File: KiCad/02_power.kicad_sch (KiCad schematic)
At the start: 48 parts, among them IC201 MCP73831T-2ACI_OT, J201 Barrel_Jack_Switch_Pin3Ring, J202 BM02B-GHS-TBT_LF__SN__N_, Q201 DMG3415U-7, U201 AMS1117-3.3, U202 TLV62569DBV

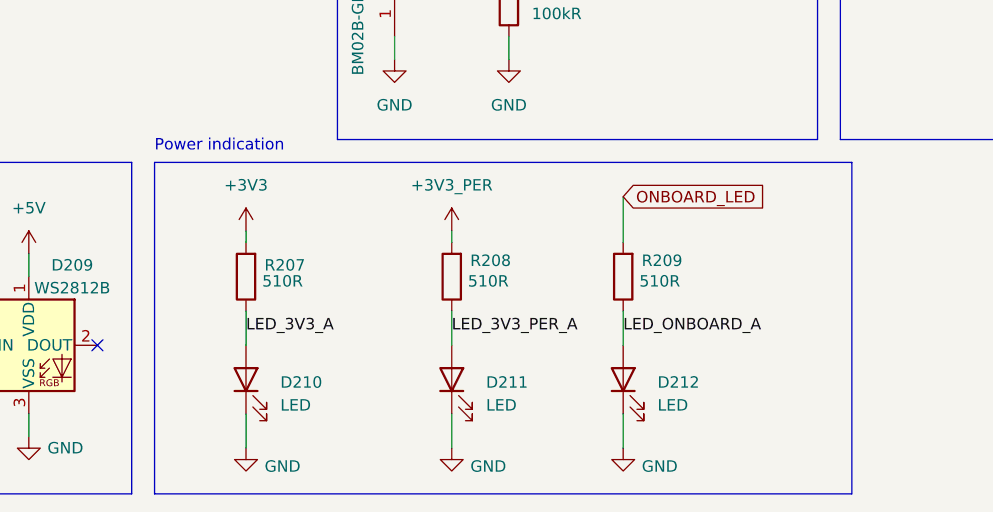
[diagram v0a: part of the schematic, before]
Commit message: Connect VBAT to ADC input to measure battery voltage
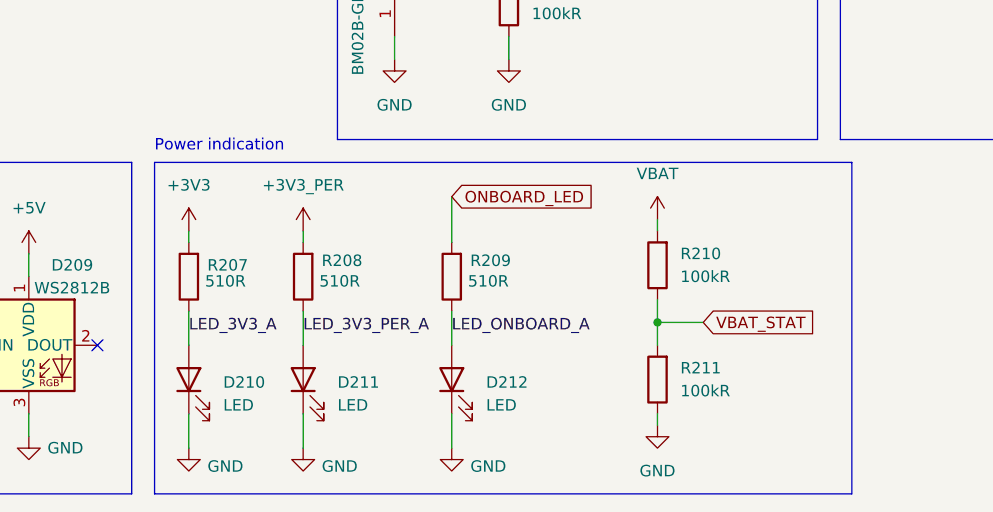
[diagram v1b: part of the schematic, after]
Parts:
- added R210, R211: 100kR, Resistor_SMD:R_0402_1005Metric, symbol Device:R
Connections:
- net GND: now also R211.1
- net VBAT: now also R210.2
- new net VBAT_STAT: R210.1, R211.2
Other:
- moved on the sheet: D210, D211, D212, R207, R208, R209

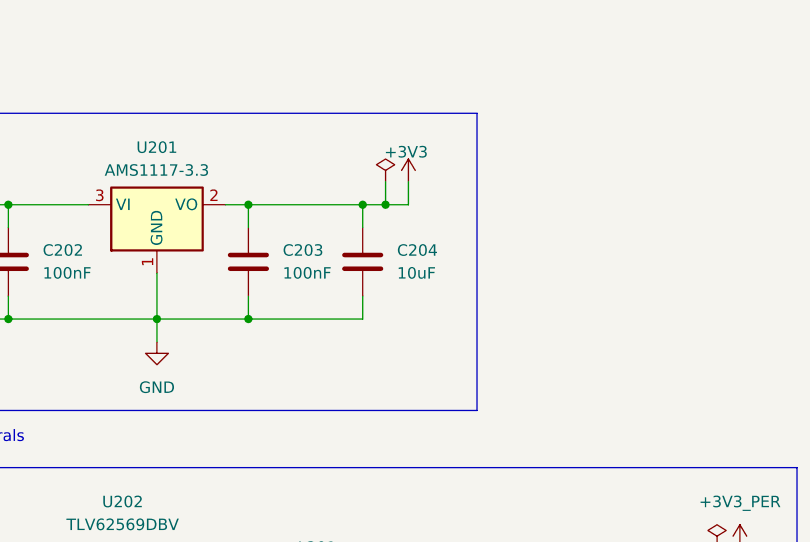
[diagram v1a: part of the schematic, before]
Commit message: Use tantalum capacitor with AMS. Add basic output to TFT.
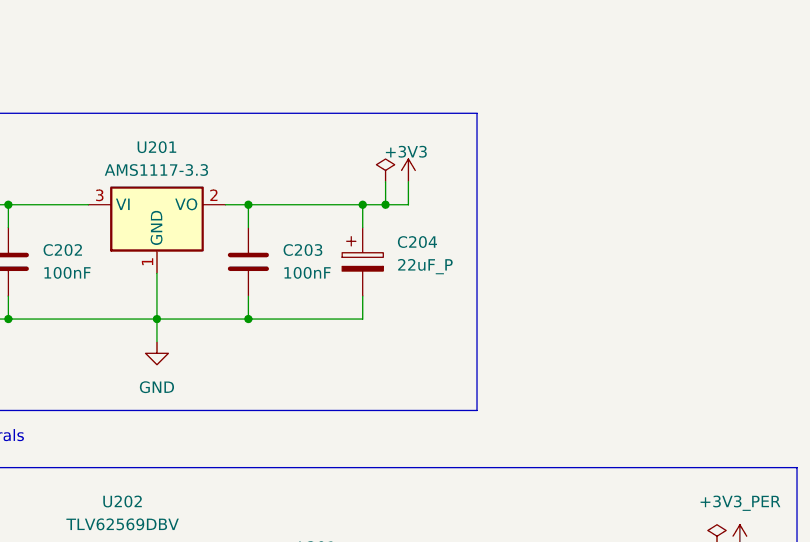
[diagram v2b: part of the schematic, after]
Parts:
- removed C204: 10uF, Capacitor_SMD:C_0603_1608Metric, symbol Device:C
- added C204: 22uF_P, Capacitor_Tantalum_SMD:CP_EIA-3216-18_Kemet-A, symbol Device:C_Polarized
- IC201: Manufacturer (none) -> MICROCHIP; Manufacturer Part Number (none) -> MCP73831T-2ACI/OT
- J202: Manufacturer (none) -> JST; Manufacturer Part Number (none) -> BM02B-GHS-TBT(LF)(SN)(N)
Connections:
- net +3V3: now also C204.1
- net GND: now also C204.2
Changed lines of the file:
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@@
 	)
 	(symbol
-		(lib_id "Device:C")
-		(at 175.26 40.64 0)
-		(unit 1)
-		(exclude_from_sim no)
-		(in_bom yes)
-		(on_board yes)
-		(dnp no)
-		(fields_autoplaced yes)
-		(property "Reference" "C204"
-			(at 179.07 39.3699 0)
-			(effects
-				(font
-					(size 1.27 1.27)
-				)
-				(justify left)
-			)
-		)
-		(property "Value" "10uF"
-			(at 179.07 41.9099 0)
-			(effects
-				(font
-					(size 1.27 1.27)
-				)
-				(justify left)
-			)
-		)
-		(property "Footprint" "Capacitor_SMD:C_0603_1608Metric"
-			(at 176.2252 44.45 0)
-			(effects
-				(font
-					(size 1.27 1.27)
-				)
-				(hide yes)
-			)
-		)
-		(property "Datasheet" "~"
-			(at 175.26 40.64 0)
-			(effects
-				(font
-					(size 1.27 1.27)
-				)
-				(hide yes)
-			)
-		)
-		(property "Description" "Unpolarized capacitor"
-			(at 175.26 40.64 0)
-			(effects
-				(font
-					(size 1.27 1.27)
-				)
-				(hide yes)
-			)
-		)
-		(property "Manufacturer" "Samsung Electro-Mechanics"
-			(at 175.26 40.64 0)
-			(effects
-				(font
-					(size 1.27 1.27)
-				)
-				(hide yes)
-			)
-		)
-		(property "Manufacturer Part Number" "CL10A106KP8NNNC"
-			(at 175.26 40.64 0)
-			(effects
-				(font
-					(size 1.27 1.27)
-				)
-				(hide yes)
-			)
-		)
-		(property "MANUFACTURER" ""
-			(at 175.26 40.64 0)
-			(effects
-				(font
-					(size 1.27 1.27)
-				)
-				(hide yes)
-			)
-		)
-		(property "PARTREV" ""
-			(at 175.26 40.64 0)
-			(effects
-				(font
-					(size 1.27 1.27)
-				)
-				(hide yes)
-			)
-		)
-		(property "STANDARD" ""
-			(at 175.26 40.64 0)
-			(effects
-				(font
-					(size 1.27 1.27)
-				)
-				(hide yes)
-			)
-		)
-		(pin "2"
-		)
-		(pin "1"
-		)
-		(instances
-			(project "esp32_s3_weather_webserver"
-				(path "/04e96486-ec4c-4881-a0bf-37cb6ce91c2d/693a6e30-8587-4c1f-a65c-fa3e0d92fd94"
-					(reference "C204")
-					(unit 1)
-				)
-			)
-		)
-	)
-	(symbol
 		(lib_id "power:GND")
 		(at 77.47 49.53 0)
@@
 	)
 	(symbol
+		(lib_id "Device:C_Polarized")
+		(at 175.26 40.64 0)
+		(unit 1)
+		(exclude_from_sim no)
+		(in_bom yes)
+		(on_board yes)
+		(dnp no)
+		(fields_autoplaced yes)
+		(property "Reference" "C204"
+			(at 179.07 38.4809 0)
+			(effects
+				(font
+					(size 1.27 1.27)
+				)
+				(justify left)
+			)
+		)
+		(property "Value" "22uF_P"
+			(at 179.07 41.0209 0)
+			(effects
+				(font
+					(size 1.27 1.27)
+				)
+				(justify left)
+			)
+		)
+		(property "Footprint" "Capacitor_Tantalum_SMD:CP_EIA-3216-18_Kemet-A"
+			(at 176.2252 44.45 0)
+			(effects
+				(font
+					(size 1.27 1.27)
+				)
+				(hide yes)
+			)
+		)
+		(property "Datasheet" "~"
+			(at 175.26 40.64 0)
+			(effects
+				(font
+					(size 1.27 1.27)
+				)
+				(hide yes)
+			)
+		)
+		(property "Description" "Polarized capacitor"
+			(at 175.26 40.64 0)
+			(effects
+				(font
+					(size 1.27 1.27)
+				)
+				(hide yes)
+			)
+		)
+		(property "Manufacturer" "Kyocera AVX"
+			(at 175.26 40.64 0)
+			(effects
+				(font
+					(size 1.27 1.27)
+				)
+				(hide yes)
+			)
+		)
+		(property "Manufacturer Part Number" "TAJA226K010RNJ"
+			(at 175.26 40.64 0)
+			(effects
+				(font
+					(size 1.27 1.27)
+				)
+				(hide yes)
+			)
+		)
+		(pin "2"
+		)
+		(pin "1"
+		)
+		(instances
+			(project ""
+				(path "/04e96486-ec4c-4881-a0bf-37cb6ce91c2d/693a6e30-8587-4c1f-a65c-fa3e0d92fd94"
+					(reference "C204")
+					(unit 1)
+				)
+			)
+		)
+	)
+	(symbol
 		(lib_id "Device:Polyfuse")
 		(at 52.07 101.6 90)
@@
 			)
 		)
+		(property "Manufacturer" "JST"
+			(at 121.92 140.97 90)
+			(effects
+				(font
+					(size 1.27 1.27)
+				)
+				(hide yes)
+			)
+		)
+		(property "Manufacturer Part Number" "BM02B-GHS-TBT(LF)(SN)(N)"
+			(at 121.92 140.97 90)
+			(effects
+				(font
+					(size 1.27 1.27)
+				)
+				(hide yes)
+			)
+		)
 		(pin "2"
 		)
@@
 				(hide yes)
 			)
+		)
+		(property "Manufacturer" "MICROCHIP"
+			(at 207.01 133.35 0)
+			(effects
+				(font
+					(size 1.27 1.27)
+				)
+				(hide yes)
+			)
+		)
+		(property "Manufacturer Part Number" "MCP73831T-2ACI/OT"
+			(at 207.01 133.35 0)
+			(effects
+				(font
+					(size 1.27 1.27)
+				)
+				(hide yes)
+			)

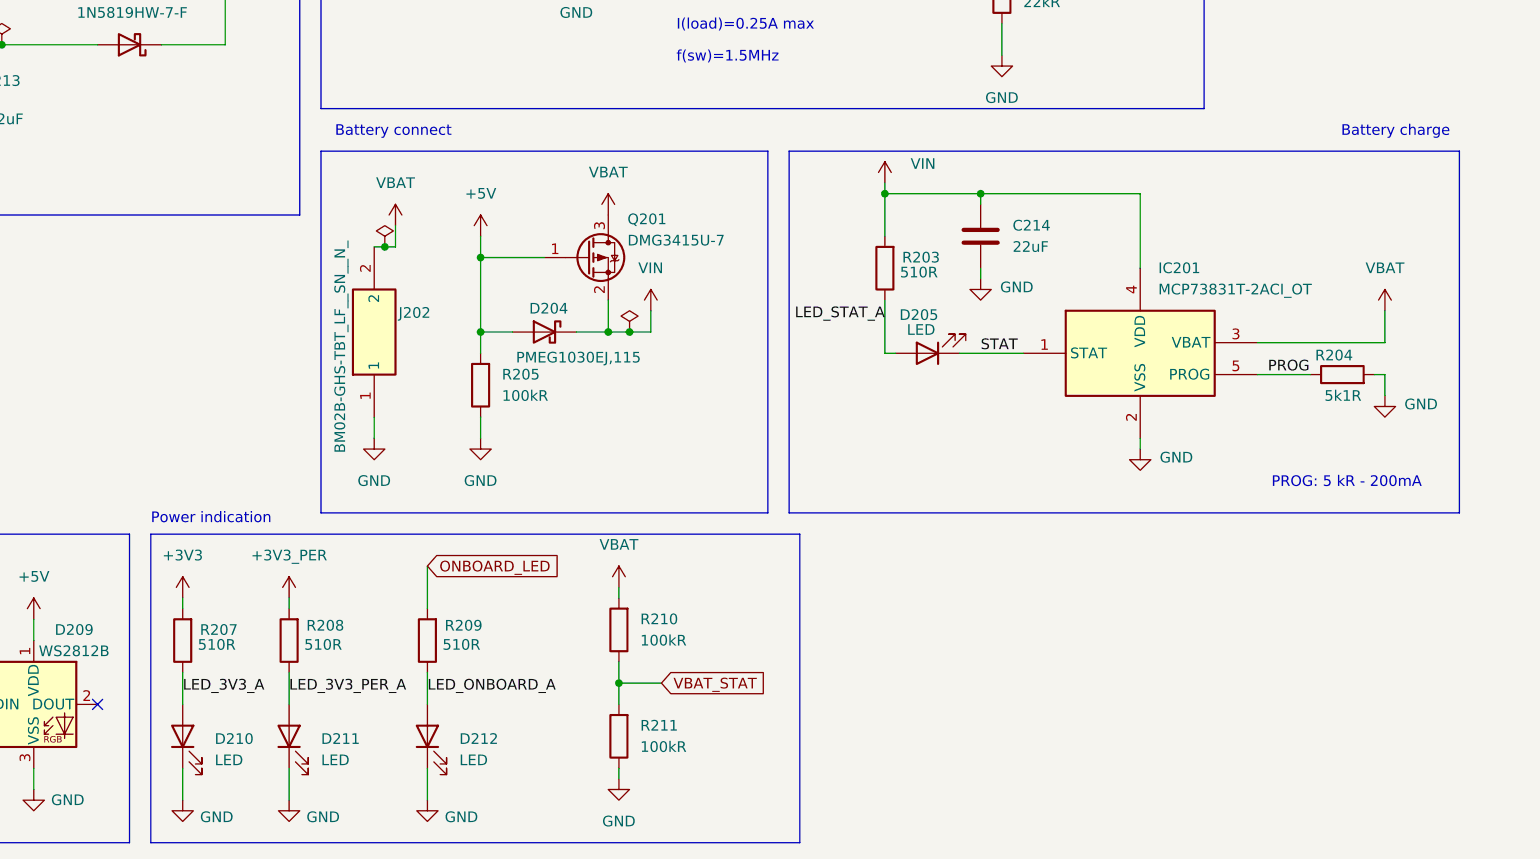
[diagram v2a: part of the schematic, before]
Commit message: VBAT decoupling capacitor
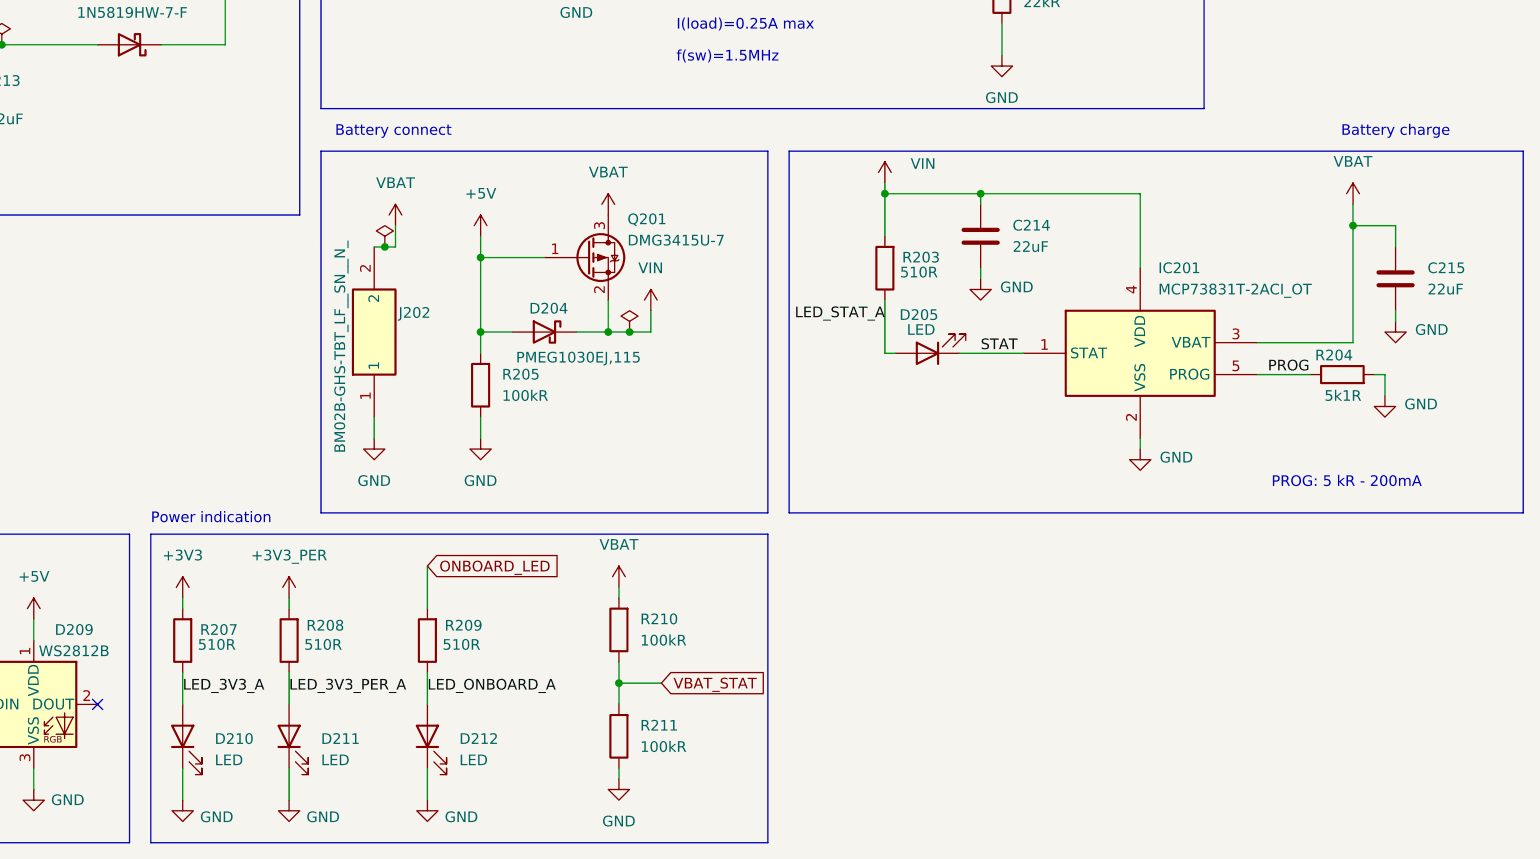
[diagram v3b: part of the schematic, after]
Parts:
- added C215: 22uF, Capacitor_SMD:C_0603_1608Metric, symbol Device:C
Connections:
- net GND: now also C215.2
- net VBAT: now also C215.1
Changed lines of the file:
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@@
 	(rectangle
 		(start 173.99 114.3)
-		(end 254 157.48)
+		(end 261.62 157.48)
 		(stroke
 			(width 0)
@@
 	(rectangle
 		(start 97.79 160.02)
-		(end 175.26 196.85)
+		(end 171.45 196.85)
 		(stroke
 			(width 0)
@@
 	)
 	(junction
+		(at 241.3 123.19)
+		(diameter 0)
+		(color 0 0 0 0)
+	)
+	(junction
 		(at 199.39 90.17)
 		(diameter 0)
@@
 	(wire
 		(pts
+			(xy 246.38 125.73) (xy 246.38 123.19)
+		)
+		(stroke
+			(width 0)
+			(type default)
+		)
+	)
+	(wire
+		(pts
 			(xy 40.64 39.37) (xy 43.18 39.37)
 		)
@@
 	(wire
 		(pts
+			(xy 241.3 123.19) (xy 246.38 123.19)
+		)
+		(stroke
+			(width 0)
+			(type default)
+		)
+	)
+	(wire
+		(pts
 			(xy 99.06 36.83) (xy 106.68 36.83)
 		)
@@
 	(wire
 		(pts
-			(xy 245.11 137.16) (xy 245.11 133.35)
+			(xy 241.3 137.16) (xy 241.3 123.19)
 		)
 		(stroke
@@
 	(wire
 		(pts
-			(xy 229.87 137.16) (xy 245.11 137.16)
+			(xy 229.87 137.16) (xy 241.3 137.16)
 		)
 		(stroke
@@
 	(wire
 		(pts
+			(xy 241.3 123.19) (xy 241.3 120.65)
+		)
+		(stroke
+			(width 0)
+			(type default)
+		)
+	)
+	(wire
+		(pts
 			(xy 111.76 69.85) (xy 109.22 69.85)
 		)
@@
 	(wire
 		(pts
+			(xy 246.38 133.35) (xy 246.38 134.62)
+		)
+		(stroke
+			(width 0)
+			(type default)
+		)
+	)
+	(wire
+		(pts
 			(xy 77.47 101.6) (xy 77.47 104.14)
 		)
@@
 	)
 	(symbol
+		(lib_id "power:GND")
+		(at 246.38 134.62 0)
+		(mirror y)
+		(unit 1)
+		(exclude_from_sim no)
+		(in_bom yes)
+		(on_board yes)
+		(dnp no)
+		(property "Reference" "#PWR0251"
+			(at 246.38 140.97 0)
+			(effects
+				(font
+					(size 1.27 1.27)
+				)
+				(hide yes)
+			)
+		)
+		(property "Value" "GND"
+			(at 250.698 135.636 0)
+			(effects
+				(font
+					(size 1.27 1.27)
+				)
+			)
+		)
+		(property "Footprint" ""
+			(at 246.38 134.62 0)
+			(effects
+				(font
+					(size 1.27 1.27)
+				)
+				(hide yes)
+			)
+		)
+		(property "Datasheet" ""
+			(at 246.38 134.62 0)
+			(effects
+				(font
+					(size 1.27 1.27)
+				)
+				(hide yes)
+			)
+		)
+		(property "Description" "Power symbol creates a global label with name \"GND\" , ground"
+			(at 246.38 134.62 0)
+			(effects
+				(font
+					(size 1.27 1.27)
+				)
+				(hide yes)
+			)
+		)
+		(pin "1"
+		)
+		(instances
+			(project "esp32_s3_weather_webserver"
+				(path "/04e96486-ec4c-4881-a0bf-37cb6ce91c2d/693a6e30-8587-4c1f-a65c-fa3e0d92fd94"
+					(reference "#PWR0251")
+					(unit 1)
+				)
+			)
+		)
+	)
+	(symbol
 		(lib_id "power:+5V")
 		(at 59.69 31.75 0)
@@
 	(symbol
 		(lib_id "power:+5V")
-		(at 245.11 133.35 0)
+		(at 241.3 120.65 0)
 		(mirror y)
 		(unit 1)
@@
 		(fields_autoplaced yes)
 		(property "Reference" "#PWR0231"
-			(at 245.11 137.16 0)
+			(at 241.3 124.46 0)
 			(effects
 				(font
@@
 		)
 		(property "Value" "VBAT"
-			(at 245.11 128.27 0)
+			(at 241.3 115.57 0)
 			(effects
 				(font
@@
 		)
 		(property "Footprint" ""
-			(at 245.11 133.35 0)
+			(at 241.3 120.65 0)
 			(effects
 				(font
@@
 		)
 		(property "Datasheet" ""
-			(at 245.11 133.35 0)
+			(at 241.3 120.65 0)
 			(effects
 				(font
@@
 		)
 		(property "Description" "Power symbol creates a global label with name \"+5V\""
-			(at 245.11 133.35 0)
+			(at 241.3 120.65 0)
 			(effects
 				(font
@@
 					(unit 1)
 				)
+			)
+		)
+	)
+	(symbol
+		(lib_id "Device:C")
+		(at 246.38 129.54 0)
+		(unit 1)
+		(exclude_from_sim no)
+		(in_bom yes)
+		(on_board yes)
+		(dnp no)
+		(property "Reference" "C215"
+			(at 250.19 128.27 0)
+			(effects
+				(font
+					(size 1.27 1.27)
+				)
+				(justify left)
+			)
+		)
+		(property "Value" "22uF"
+			(at 250.19 130.81 0)
+			(effects
+				(font
+					(size 1.27 1.27)
+				)
+				(justify left)
+			)
+		)
+		(property "Footprint" "Capacitor_SMD:C_0603_1608Metric"
+			(at 247.3452 133.35 0)
+			(effects
+				(font
+					(size 1.27 1.27)
+				)
+				(hide yes)
+			)
+		)
+		(property "Datasheet" "~"
+			(at 246.38 129.54 0)
+			(effects
+				(font
+					(size 1.27 1.27)
+				)
+				(hide yes)
+			)
+		)
+		(property "Description" ""
+			(at 246.38 129.54 0)
+			(effects
+				(font
+					(size 1.27 1.27)
+				)
+				(hide yes)
+			)
+		)
+		(property "Manufacturer" "Samsung Electro-Mechanics"
+			(at 246.38 129.54 0)
+			(effects
+				(font
+					(size 1.27 1.27)
+				)
+				(hide yes)
+			)
+		)
+		(property "Manufacturer Part Number" "CL10A226MP8NUNE"
+			(at 246.38 129.54 0)
+			(effects
+				(font
+					(size 1.27 1.27)
+				)
+				(hide yes)
+			)
+		)
+		(property "MANUFACTURER" ""
+			(at 246.38 129.54 0)
+			(effects
+				(font
+					(size 1.27 1.27)
+				)
+				(hide yes)
+			)
+		)
+		(property "PARTREV" ""
+			(at 246.38 129.54 0)
+			(effects
+				(font
+					(size 1.27 1.27)
+				)
+				(hide yes)
+			)
+		)
+		(property "STANDARD" ""
+			(at 246.38 129.54 0)
+			(effects
+				(font
+					(size 1.27 1.27)
+				)
+				(hide yes)
+			)
+		)
+		(pin "1"
+		)
+		(pin "2"
+		)
+		(instances
+			(project "esp32_s3_weather_webserver"
+				(path "/04e96486-ec4c-4881-a0bf-37cb6ce91c2d/693a6e30-8587-4c1f-a65c-fa3e0d92fd94"
+					(reference "C215")
+					(unit 1)
+				)

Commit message: Production files prepare
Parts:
- FB201, FB202, FB203: Manufacturer Murata Electronics -> muRata
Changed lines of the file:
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@@
 			)
 		)
-		(property "Manufacturer" "Murata Electronics"
+		(property "Manufacturer" "muRata"
 			(at 68.58 69.85 0)
 			(effects
@@
 			)
 		)
-		(property "Manufacturer" "Murata Electronics"
+		(property "Manufacturer" "muRata"
 			(at 68.58 101.6 0)
 			(effects
@@
 			)
 		)
-		(property "Manufacturer" "Murata Electronics"
+		(property "Manufacturer" "muRata"
 			(at 68.58 36.83 0)
 			(effects
